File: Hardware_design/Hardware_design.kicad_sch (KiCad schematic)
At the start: 0 parts

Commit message: component_search_finidhed
starting to design schematics
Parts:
- added IC?: ESP32-S3-WROOM-1-N16, ESP32S3WROOM1N16, symbol ESP32-S3-WROOM-1-N16:ESP32-S3-WROOM-1-N16
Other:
- added sheet Display_management (Display_management.kicad_sch)

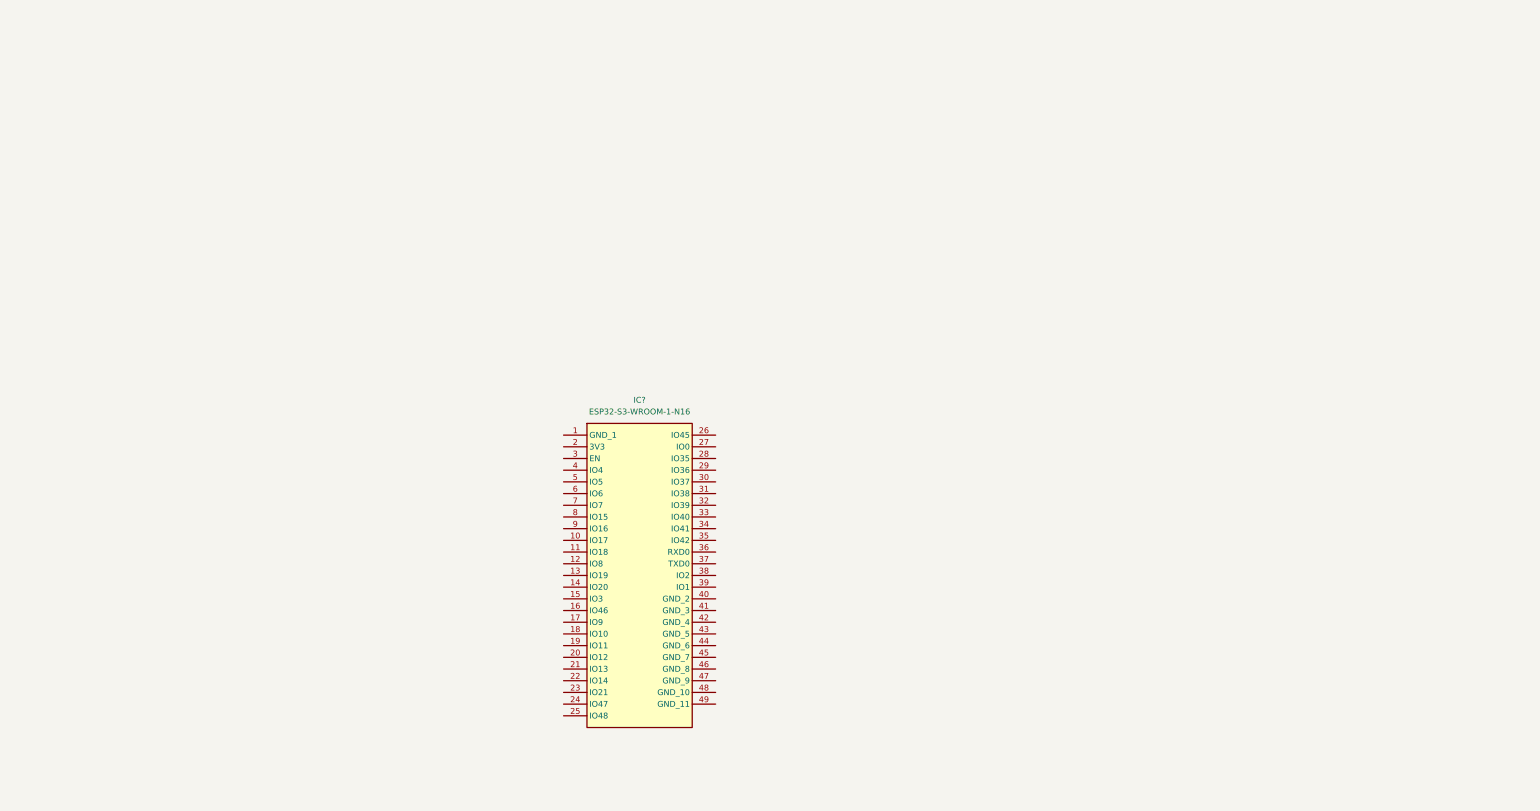
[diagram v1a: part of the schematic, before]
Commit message: INDEX INTERRUPTION working
the device has been configured for transfering the cntr reg count data to the otr reg so it stores data at a precise moment so when we want to read it later with the esp32se we get the count at that exact time
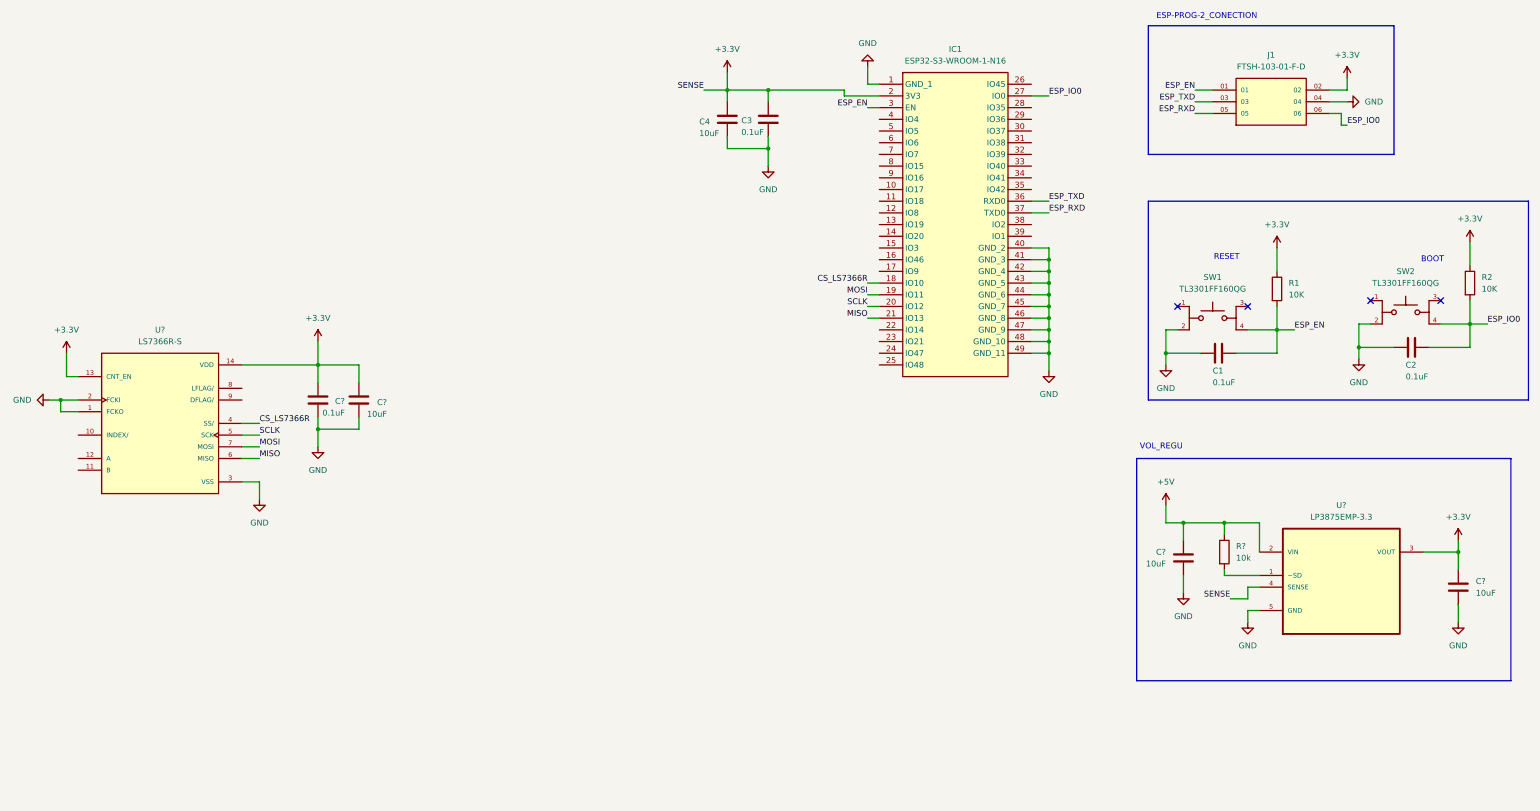
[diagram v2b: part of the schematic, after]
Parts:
- added C1, C2, C3, C?: 0.1uF, symbol Device:C
- added C4, C? (x3): 10uF, symbol Device:C
- added J1: FTSH-103-01-F-D, FTSH-103-01-F-D:SAMTEC_FTSH-103-01-F-D, symbol PROG_CONECTOR_FTSH-103-01-F-D:FTSH-103-01-F-D
- added R1, R2: 10K, symbol Device:R
- added R?: 10k, symbol Device:R
- added SW1, SW2: TL3301FF160QG, TL3301FF160QG:SW_TL3301FF160QG, symbol BUTTON_TL3301FF160QG:TL3301FF160QG
- added U?: LS7366R-S, LS7366R-S:SOIC127P600X175-14N, symbol LS7366R-S:LS7366R-S
- added U?: LP3875EMP-3.3, LP3875EMP-3.3:SOT15P696X180-5N, symbol V_REGU_LP3875EMP-3.3:LP3875EMP-3.3
- gave numbers to parts that had none: 1
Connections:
- net GND: now reaches IC1.1 (GND_1)
- net GND: now also IC1.40 (GND_2), IC1.41 (GND_3), IC1.42 (GND_4), IC1.43 (GND_5), IC1.44 (GND_6), IC1.45 (GND_7), IC1.46 (GND_8), IC1.47 (GND_9), IC1.48 (GND_10), IC1.49 (GND_11), C1.2, C2.2, C3.2, C4.2, C?.2, C?.2, C?.2, C?.2, J1.04, SW1.2, SW2.2, U?.1 (FCKO), U?.2 (FCKI), U?.3 (VSS), U?.5 (GND)
- net CS_LS7366R: now reaches IC1.18 (IO10)
- net CS_LS7366R: now also U?.4 (SS/)
- net MOSI: now reaches IC1.19 (IO11)
- net MOSI: now also U?.7 (MOSI)
- net +3.3V: now reaches IC1.2 (3V3)
- net +3.3V: now also C3.1, C4.1, C?.1, C?.1, C?.1, J1.02, R1.1, R2.1, U?.13 (CNT_EN), U?.14 (VDD), U?.3 (VOUT), U?.4 (SENSE)
- net SCLK: now reaches IC1.20 (IO12)
- net SCLK: now also U?.5 (SCK)
- net MISO: now reaches IC1.21 (IO13)
- net MISO: now also U?.6 (MISO)
- net ESP_IO0: now reaches IC1.27 (IO0)
- net ESP_IO0: now also C2.1, J1.06, R2.2, SW2.4
- net ESP_EN: now reaches IC1.3 (EN)
- net ESP_EN: now also C1.1, J1.01, R1.2, SW1.4
- net ESP_TXD: now reaches IC1.36 (RXD0)
- net ESP_TXD: now also J1.03
- net ESP_RXD: now reaches IC1.37 (TXD0)
- net ESP_RXD: now also J1.05
- new net: R?.2, U?.1 (~SD)
- new net +5V: C?.1, R?.1, U?.2 (VIN)
- no-connect marks 0 -> 4
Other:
- note added: "BOOT"
- note added: "ESP-PROG-2_CONECTION"
- note added: "RESET"
- note added: "VOL_REGU"
- moved on the sheet: IC1

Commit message: schematic progress
saving schematic progress, butons added but a change is pending to use 10 buttons instead of 15
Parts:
- added C?: 1 uF, symbol Device:C
- added C? (x2): 15 pF, symbol Device:C
- added D?: BAT54S, BAT54S:P200_SOT-23, symbol Schottky_diode_BAT54S:BAT54S
- added E?: 1-1337445-0, 1-1337445-0:TE_1-1337445-0, symbol VNC_CONECTOR_1-1337445-0:1-1337445-0
- added R? (x6): 10k, symbol Device:R
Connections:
- net +3.3V: now also D?.2 (C), R?.1, R?.1, R?.1, R?.1, R?.1, R?.1; no longer U?.13 (CNT_EN)
- net ESP_EN: now also C?.1, R?.2
- net GND: now also C?.2, C?.2, D?.1 (A), E?.SH1 (GND), E?.SH2 (GND), E?.SH3 (GND), E?.SH4 (GND)
- net RESET_1_FILTERED: now reaches IC1.10 (IO17)
- net START_2_FILTERED: now reaches IC1.11 (IO18)
- net PAUSE_2_FILTERED: now reaches IC1.12 (IO8)
- net RESET_2_FILTERED: now reaches IC1.15 (IO3)
- net START_3_FILTERED: now reaches IC1.17 (IO9)
- net PAUSE_3_FILTERED: now reaches IC1.22 (IO14)
- net RESET_3_FILTERED: now reaches IC1.23 (IO21)
- net START_4_FILTERED: now reaches IC1.24 (IO47)
- net PAUSE_4_FILTERED: now reaches IC1.25 (IO48)
- net RESET_4_FILTERED: now reaches IC1.28 (IO35)
- net START_5_FILTERED: now reaches IC1.29 (IO36)
- net PAUSE_5_FILTERED: now reaches IC1.38 (IO2)
- net RESET_5_FILTERED: now reaches IC1.39 (IO1)
- net LFLAG: now reaches IC1.4 (IO4)
- net LFLAG: now also U?.8 (LFLAG/), R?.2
- net SCK_MAX7221: now reaches IC1.5 (IO5)
- net MOSI_MAX7221: now reaches IC1.6 (IO6)
- net CS_MAX7221: now reaches IC1.7 (IO7)
- net START_1_FILTERED: now reaches IC1.8 (IO15)
- net PAUSE_1_FILTERED: now reaches IC1.9 (IO16)
- net INDEX: now reaches U?.10 (INDEX/)
- net INDEX: now also C?.1, R?.2
- net at U?.11 (B): now also R?.2
- net Pulse_Signal: now reaches U?.12 (A)
- net Pulse_Signal: now also C?.1, D?.3, E?.1 (SIG), R?.2
- net MISO renamed MISO_LS7366R
- net MOSI renamed MOSI_LS7366R
- net SCLK renamed SCLK_LS7366R
- new net: R?.2, U?.13 (CNT_EN)
- no-connect marks 4 -> 5
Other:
- added sheet Buttons_circuits (Buttons_circuits.kicad_sch)
- note added: "Boot and reset buttons"
- note added: "Counter"
- moved on the sheet: C3, C4, C?, U?

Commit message: Buttons number modified
now the buttons are 10, one is for starting and stoping the count and another one for reseting it
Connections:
- net PAUSE_1_FILTERED is gone; now on net RESET_1_FILTERED: IC1.9 (IO16)
- net PAUSE_4_FILTERED is gone; now on net RESET_5_FILTERED: IC1.25 (IO48)
- net START_2_FILTERED is gone; now on net RESET_2_FILTERED: IC1.11 (IO18)
- net RESET_1_FILTERED: no longer IC1.10 (IO17)
- net RESET_2_FILTERED: no longer IC1.15 (IO3)
- net RESET_3_FILTERED: now also IC1.15 (IO3); no longer IC1.23 (IO21)
- net RESET_4_FILTERED: now also IC1.23 (IO21); no longer IC1.28 (IO35)
- net RESET_5_FILTERED: no longer IC1.39 (IO1)
- net PAUSE_2_FILTERED renamed START_STOP_3_FILTERED
- net PAUSE_3_FILTERED renamed START_STOP_4_FILTERED
- net PAUSE_5_FILTERED: no longer names the net of IC1.38 (IO2)
- net START_1_FILTERED renamed START_STOP_1_FILTERED
- net START_3_FILTERED: no longer names the net of IC1.17 (IO9)
- net START_4_FILTERED renamed START_STOP_5_FILTERED
- net START_5_FILTERED: no longer names the net of IC1.29 (IO36)
- new net START_STOP_2_FILTERED: IC1.10 (IO17)
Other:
- sheet Buttons_circuits ports: added START_STOP_1_FILTERED, START_STOP_2_FILTERED, START_STOP_3_FILTERED, START_STOP_4_FILTERED, START_STOP_5_FILTERED; removed PAUSE_1_FILTERED, PAUSE_2_FILTERED, PAUSE_3_FILTERED, PAUSE_4_FILTERED, PAUSE_5_FILTERED, START_1_FILTERED, START_2_FILTERED, START_3_FILTERED, START_4_FILTERED, START_5_FILTERED
- sheet Display_management ports: added CS_MAX7221, MOSI_MAX7221, SCK_MAX7221; removed none
- moved on the sheet: C3, C4

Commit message: starting footprint asignment
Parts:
- added C10, C37, C9: 0.1 uF, Footprints:0805_SMD_CERAMIC_CAP_T491B106K016AT, symbol Device:C
- added C35, C36: 10uF, Footprints:0805_SMD_TANT_CAP_T491B106K016AT, symbol Device:C
- added D2: LTST-C170KGKT, Footprints:GREEN_LED_LTST-C170KGKT, symbol GREEN_LED_LTST-C170KGKT:LTST-C170KGKT
- added J2: SBH11-PBPC-D05-ST-BK, Footprints:JTAG_2.54_SBH11-PBPC-D05-ST-BK, symbol JTAG_2.54_SBH11-PBPC-D05-ST-BK:SBH11-PBPC-D05-ST-BK
- added J3: 54-00131, Footprints:POWER_CONE_54-00131, symbol POWER_CONE_54-00131:54-00131
- added R8: 10k, symbol Device:R
- added R9: 68, symbol Device:R
- added TP1, TP2, TP3, TP4, TP5, TP6, TP7: TestPoint, symbol Connector:TestPoint
- added U2: TXB0104DR, Footprints:LEVEL_SHIFTER_TXB0104DR, symbol LEVEL_SHIFTER_TXB0104DR:TXB0104DR
- C1, C2, C3: footprint (none) -> Footprints:0805_SMD_CERAMIC_CAP_T491B106K016AT
- C12, C13, C8: renamed from C?; footprint (none) -> Footprints:0805_SMD_TANT_CAP_T491B106K016AT
- C4: footprint (none) -> Footprints:0805_SMD_TANT_CAP_T491B106K016AT
- C5, C6, C7: renamed from C?; footprint (none) -> Footprints:0805_SMD_CERAMIC_CAP_T491B106K016AT
- D1: renamed from D?; footprint BAT54S:P200_SOT-23 -> Footprints:Schottky_diode_BAT54S
- E1: renamed from E?; footprint 1-1337445-0:TE_1-1337445-0 -> Footprints:VNC_CONECTOR_1-1337445-0
- IC1: footprint ESP32S3WROOM1N16 -> Footprints:ESP32S3WROOM1N16
- J1: footprint FTSH-103-01-F-D:SAMTEC_FTSH-103-01-F-D -> Footprints:PROG_CONECTOR_SAMTEC_FTSH-103-01-F-D
- SW1, SW2: footprint TL3301FF160QG:SW_TL3301FF160QG -> Footprints:BUTTON_TL3301FF160QG
- U1: renamed from U?; footprint LS7366R-S:SOIC127P600X175-14N -> Footprints:LS7366R-S
- U3: renamed from U?; footprint LP3875EMP-3.3:SOT15P696X180-5N -> Footprints:V_REGU_LP3875EMP-3.3
- gave numbers to parts that had none: 8
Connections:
- net +3.3V: now also C35.1, C9.1, J2.1, R9.1, TP2.1, U2.1 (VCCA)
- net +5V: now also C10.1, C36.1, C37.1, J3.A, TP1.1, U2.14 (VCCB)
- net CS_MAX7221: now also U2.4 (A3)
- net GND: now also C11.2, C10.2, C35.2, C36.2, C37.2, C9.2, D2.-, J2.3, J2.5, J2.7, J2.9, J3.B, J3.C, R8.2, TP3.1, U2.7 (GND)
- net INDEX: now also TP5.1
- net LFLAG: now also TP6.1
- net MOSI_MAX7221: now also U2.3 (A2)
- net Pulse_Signal: now also TP4.1
- net SCK_MAX7221: now also U2.2 (A1)
- net ESP_TCK: now reaches IC1.32 (IO39)
- net ESP_TCK: now also J2.4
- net ESP_TDO: now reaches IC1.33 (IO40)
- net ESP_TDO: now also J2.6
- net ESP_TDI: now reaches IC1.34 (IO41)
- net ESP_TDI: now also J2.8
- net ESP_TMS: now reaches IC1.35 (IO42)
- net ESP_TMS: now also J2.2
- net OE: now reaches IC1.39 (IO1)
- net OE: now also R8.1, TP7.1, U2.8 (OE)
- new net: D2.+, R9.2
- new net CS_MAX7221_5V: U2.11 (B3)
- new net MOSI_MAX7221_5V: U2.12 (B2)
- new net SCK_MAX7221_5V: U2.13 (B1)
- no-connect marks 5 -> 18
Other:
- sheet Display_management ports: added CS_MAX7221_5V, MOSI_MAX7221_5V, SCK_MAX7221_5V; removed CS_MAX7221, MOSI_MAX7221, SCK_MAX7221
- note added: "JTAG"
- moved on the sheet: C12, C13, R11, U3

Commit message: all footprints asigned
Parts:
- C11: footprint (none) -> Footprints:0805_SMD_CERAMIC_CAP_T491B106K016AT
- R1, R10, R11, R2, R3, R4, R5, R6, R7, R8, R9: footprint (none) -> Footprints:0805_RES_RESC2012X60N
- TP1, TP2, TP3, TP4, TP5, TP6, TP7: footprint (none) -> TestPoint:TestPoint_Pad_1.0x1.0mm
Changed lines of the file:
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@@
 			)
 		)
-		(property "Footprint" ""
+		(property "Footprint" "TestPoint:TestPoint_Pad_1.0x1.0mm"
 			(at 33.02 166.37 0)
 			(hide yes)
@@
 			)
 		)
-		(property "Footprint" ""
+		(property "Footprint" "Footprints:0805_RES_RESC2012X60N"
 			(at 60.452 59.69 90)
 			(hide yes)
@@
 			)
 		)
-		(property "Footprint" ""
+		(property "Footprint" "Footprints:0805_RES_RESC2012X60N"
 			(at 201.422 30.48 90)
 			(hide yes)
@@
 			)
 		)
-		(property "Footprint" ""
+		(property "Footprint" "Footprints:0805_SMD_CERAMIC_CAP_T491B106K016AT"
 			(at 202.2348 50.8 0)
 			(hide yes)
@@
 			)
 		)
-		(property "Footprint" ""
+		(property "Footprint" "TestPoint:TestPoint_Pad_1.0x1.0mm"
 			(at 33.02 139.7 0)
 			(hide yes)
@@
 			)
 		)
-		(property "Footprint" ""
+		(property "Footprint" "Footprints:0805_RES_RESC2012X60N"
 			(at 121.412 38.1 90)
 			(hide yes)
@@
 			)
 		)
-		(property "Footprint" ""
+		(property "Footprint" "Footprints:0805_RES_RESC2012X60N"
 			(at 79.502 50.8 90)
 			(hide yes)
@@
 			)
 		)
-		(property "Footprint" ""
+		(property "Footprint" "TestPoint:TestPoint_Pad_1.0x1.0mm"
 			(at 33.02 130.81 0)
 			(hide yes)
@@
 			)
 		)
-		(property "Footprint" ""
+		(property "Footprint" "Footprints:0805_RES_RESC2012X60N"
 			(at 344.932 85.09 90)
 			(hide yes)
@@
 			)
 		)
-		(property "Footprint" ""
+		(property "Footprint" "Footprints:0805_RES_RESC2012X60N"
 			(at 69.342 60.96 90)
 			(hide yes)
@@
 			)
 		)
-		(property "Footprint" ""
+		(property "Footprint" "Footprints:0805_RES_RESC2012X60N"
 			(at 52.832 60.96 90)
 			(hide yes)
@@
 			)
 		)
-		(property "Footprint" ""
+		(property "Footprint" "Footprints:0805_RES_RESC2012X60N"
 			(at 336.042 152.4 90)
 			(hide yes)
@@
 			)
 		)
-		(property "Footprint" ""
+		(property "Footprint" "Footprints:0805_RES_RESC2012X60N"
 			(at 386.842 83.82 90)
 			(hide yes)
@@
 			)
 		)
-		(property "Footprint" ""
+		(property "Footprint" "TestPoint:TestPoint_Pad_1.0x1.0mm"
 			(at 33.02 157.48 0)
 			(hide yes)
@@
 			)
 		)
-		(property "Footprint" ""
+		(property "Footprint" "TestPoint:TestPoint_Pad_1.0x1.0mm"
 			(at 33.02 148.59 0)
 			(hide yes)
@@
 			)
 		)
-		(property "Footprint" ""
+		(property "Footprint" "TestPoint:TestPoint_Pad_1.0x1.0mm"
 			(at 33.02 113.03 0)
 			(hide yes)
@@
 			)
 		)
-		(property "Footprint" ""
+		(property "Footprint" "Footprints:0805_RES_RESC2012X60N"
 			(at 184.912 64.77 90)
 			(hide yes)
@@
 			)
 		)
-		(property "Footprint" ""
+		(property "Footprint" "Footprints:0805_RES_RESC2012X60N"
 			(at 122.682 148.59 90)
 			(hide yes)
@@
 			)
 		)
-		(property "Footprint" ""
+		(property "Footprint" "TestPoint:TestPoint_Pad_1.0x1.0mm"
 			(at 33.02 121.92 0)
 			(hide yes)
